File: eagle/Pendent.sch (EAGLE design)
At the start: 39 parts, among them Q1 CMA-4544PF-W, Q2 MPSA42, Q3 8/16/20MHz, U1 MAX9814TDFN14, U2 LF50ABDT-TR, U3 ATMEGA328

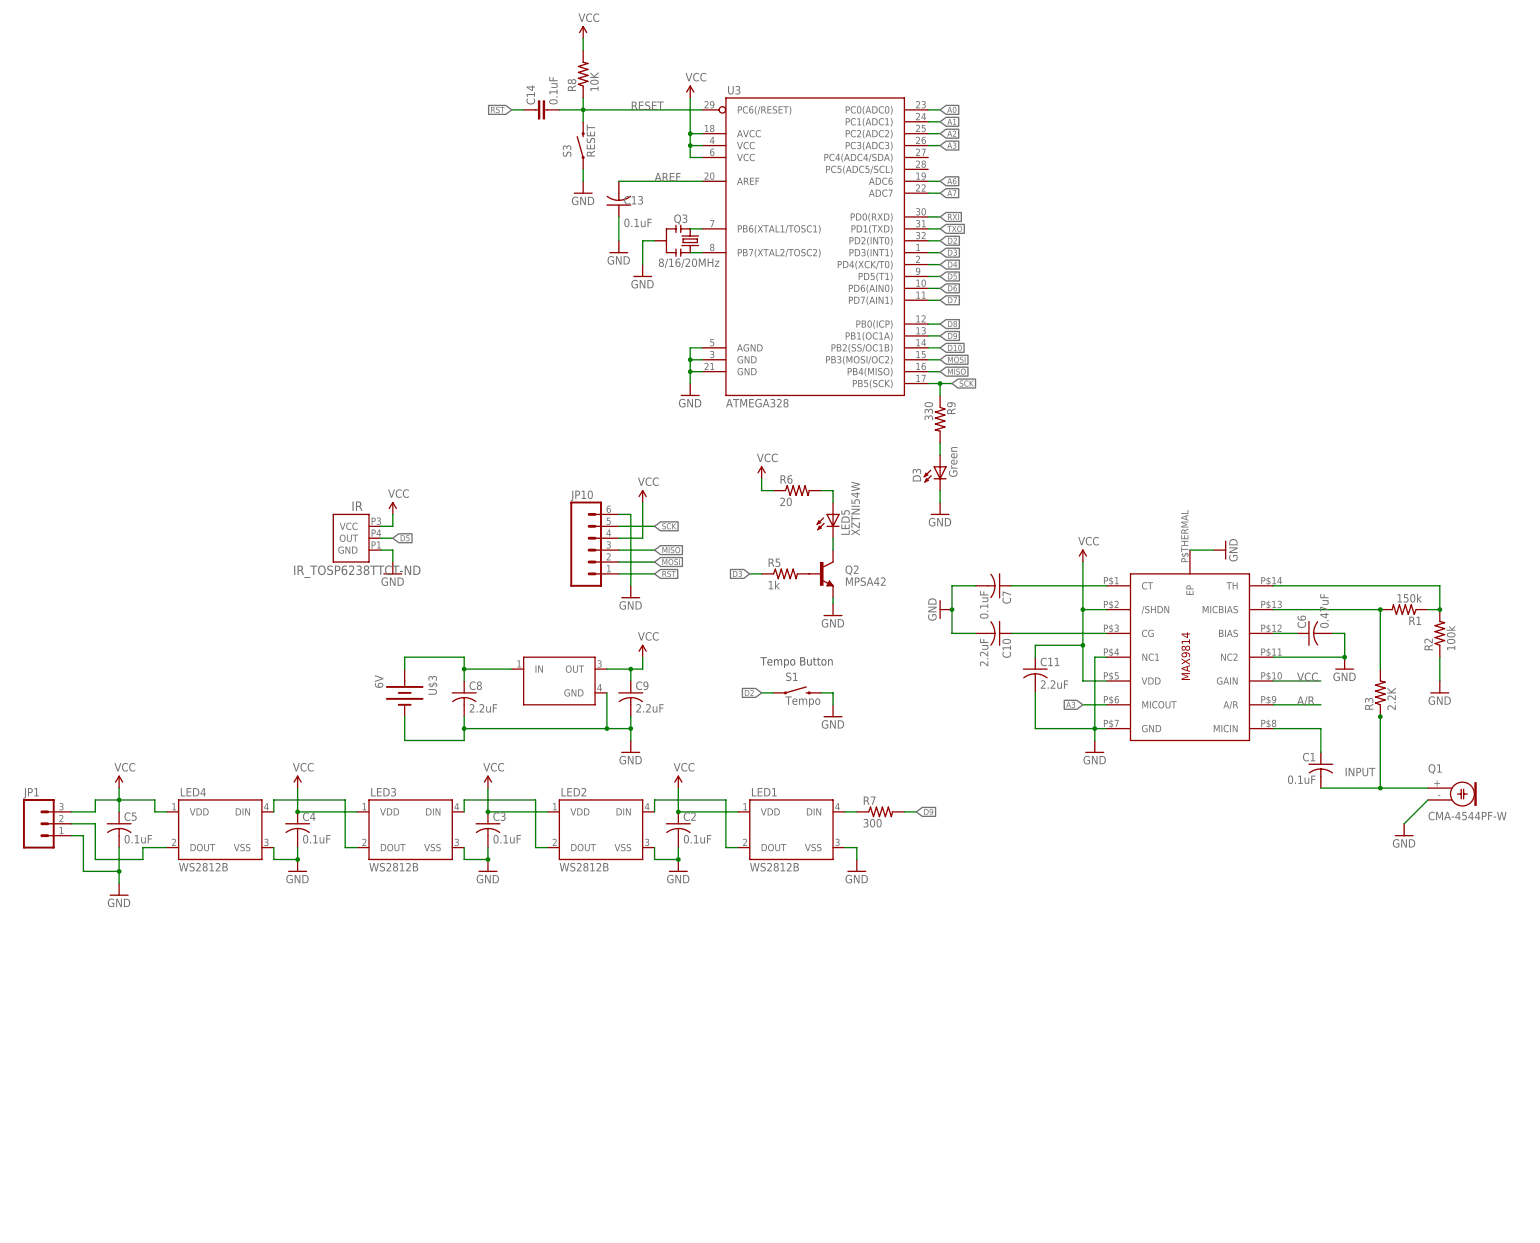
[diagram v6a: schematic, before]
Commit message: Add Push On Button
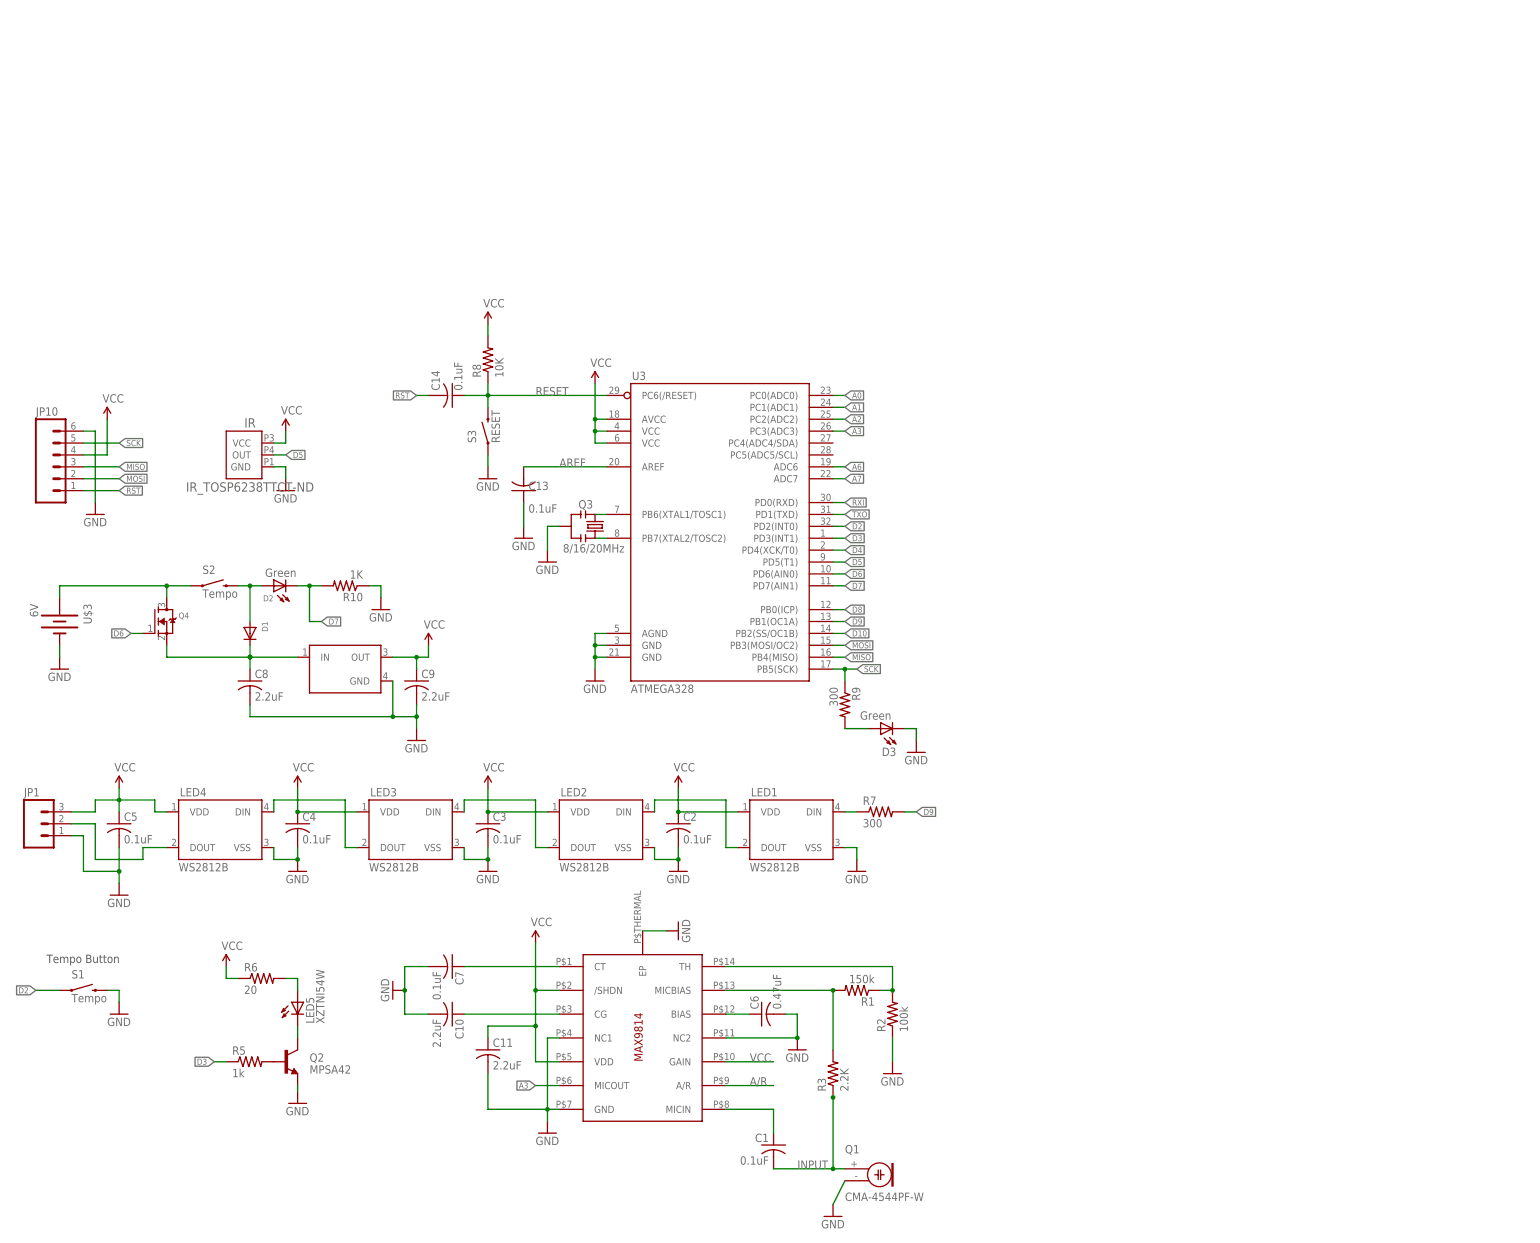
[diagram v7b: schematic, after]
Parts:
- added D1: (no value), adafruit:DIODESMA
- added D2: Green, adafruit:LEDCHIPLED_0805
- added Q4: (no value), adafruit:MOSFET-NREFLOW
- added R10: 1K, adafruit:R-US_R0805
- added S2: Tempo, SparkFun-Electromechanical:SWITCH-MOMENTARY-2SMD-REDUNDANT
- C14: device SparkFun:CAP0603-CAP -> adafruit:C-USC0805K
- R9: value 330 -> 300
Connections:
- removed net VBATT: C8.1, U$3.+, U2.IN
- new net N$20: D1.A, D2.A, S2.2
- new net VBAT: Q4.D, S2.1, U$3.+
- new net VIN: C8.1, D1.C, Q4.S, U2.IN
- net D6: now also Q4.G
- net D7: now also D2.C, R10.2
- net GND: now also R10.1
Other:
- moved on the sheet: C1, C10, C11, C13, C14, C6, C7, C8, C9, D3, IR, JP10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

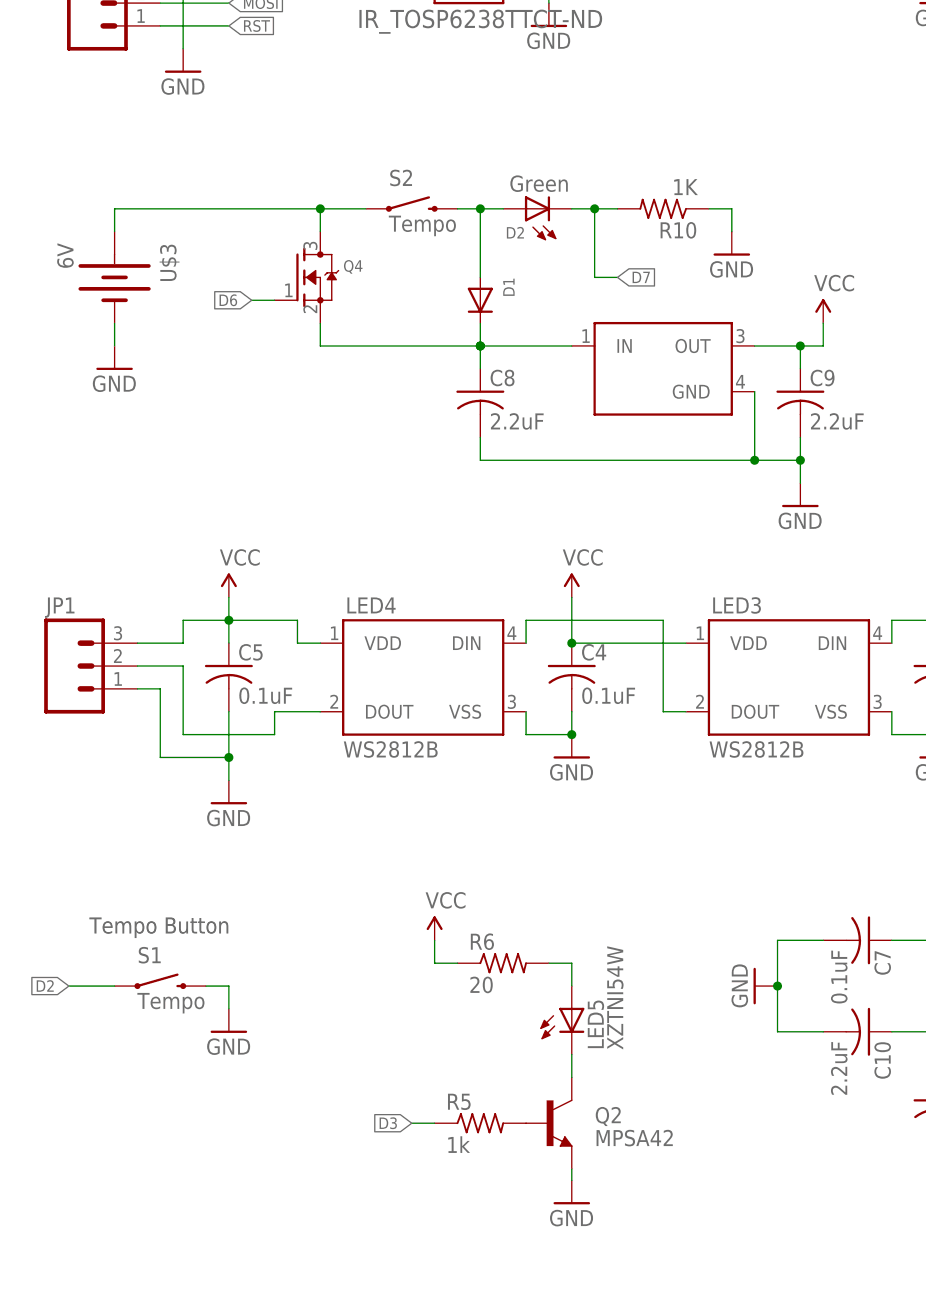
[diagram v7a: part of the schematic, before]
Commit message: Remove non-working mosfet, switch to using power down
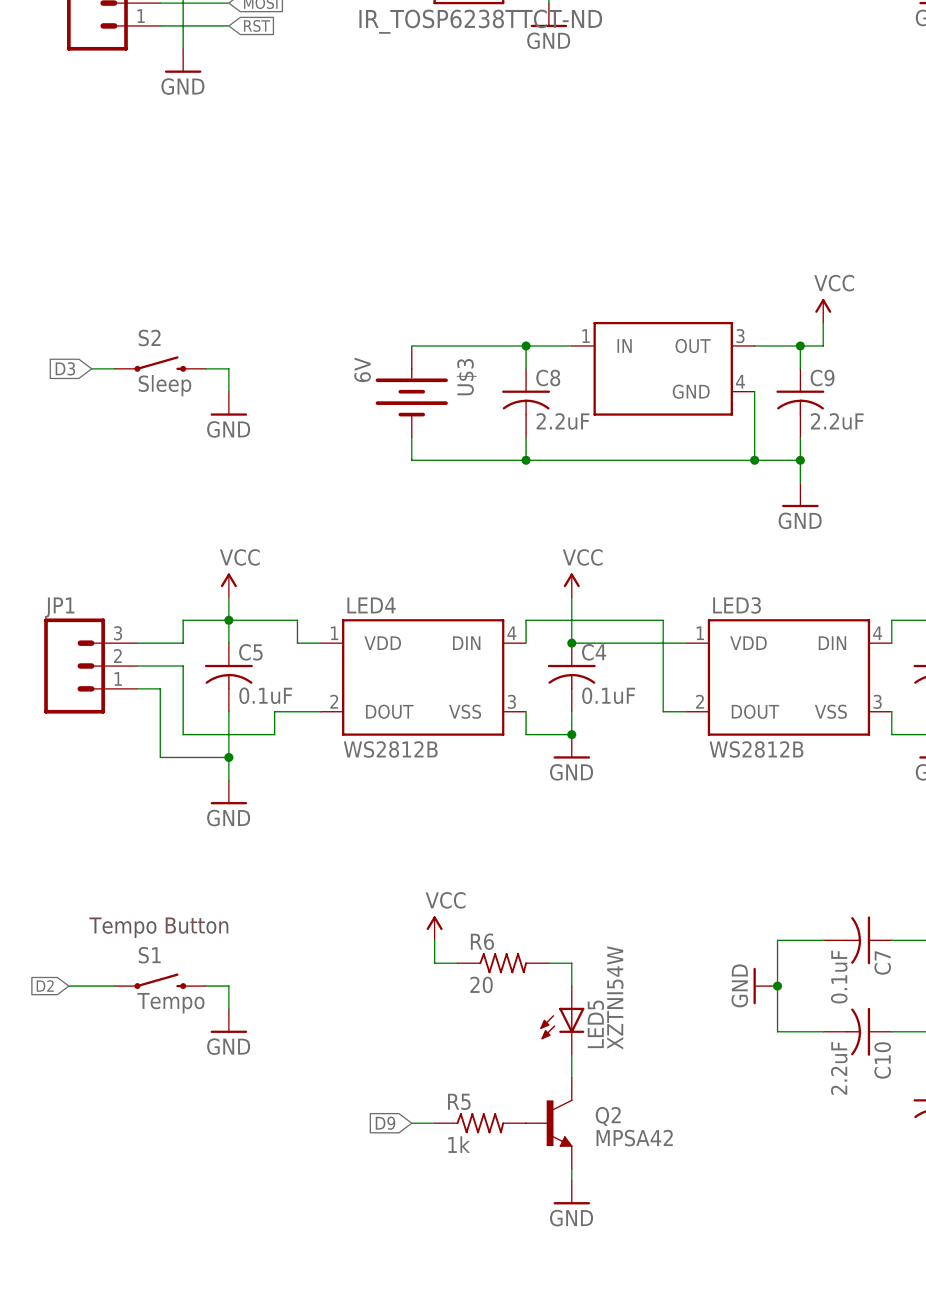
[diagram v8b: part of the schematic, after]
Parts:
- removed D1: (no value), adafruit:DIODESMA
- removed D2: Green, adafruit:LEDCHIPLED_0805
- removed Q4: (no value), adafruit:MOSFET-NREFLOW
- removed R10: 1K, adafruit:R-US_R0805
- S2: value Tempo -> Sleep
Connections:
- removed net N$20: D1.A, D2.A, S2.2
- removed net VBAT: Q4.D, S2.1, U$3.+
- net D3: now also S2.1; no longer R5.1
- net D6: no longer Q4.G
- net D7: no longer D2.C, R10.2
- net D9: now also R5.1
- net GND: now also S2.2; no longer R10.1
- net VIN: now also U$3.+; no longer D1.C, Q4.S
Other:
- moved on the sheet: C8, S2, U$3
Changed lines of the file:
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@@
 <part name="SUPPLY1" library="SparkFun-Aesthetics" deviceset="VCC" device=""/>
 <part name="GND17" library="SparkFun-Aesthetics" deviceset="GND" device=""/>
-<part name="Q4" library="adafruit" deviceset="MOSFET-N" device="REFLOW"/>
-<part name="S2" library="SparkFun-Electromechanical" deviceset="SWITCH-MOMENTARY-2" device="SMD-REDUNDANT" value="Tempo"/>
-<part name="D1" library="adafruit" deviceset="DIODE" device="SMA"/>
-<part name="D2" library="adafruit" deviceset="LED" device="CHIPLED_0805" value="Green"/>
-<part name="R10" library="adafruit" deviceset="R-US_" device="R0805" value="1K"/>
+<part name="S2" library="SparkFun-Electromechanical" deviceset="SWITCH-MOMENTARY-2" device="SMD-REDUNDANT" value="Sleep"/>
 <part name="GND23" library="SparkFun" deviceset="GND" device=""/>
-<part name="GND22" library="SparkFun" deviceset="GND" device=""/>
 </parts>
 <sheets>
@@
 <instance part="C5" gate="G$1" x="-22.86" y="114.3"/>
 <instance part="U2" gate="G$1" x="25.4" y="147.32"/>
-<instance part="U$3" gate="G$1" x="-35.56" y="157.48" rot="R270"/>
-<instance part="C8" gate="G$1" x="5.08" y="144.78"/>
+<instance part="U$3" gate="G$1" x="-2.54" y="144.78" rot="R270"/>
+<instance part="C8" gate="G$1" x="10.16" y="144.78"/>
 <instance part="C9" gate="G$1" x="40.64" y="144.78"/>
 <instance part="C1" gate="G$1" x="116.84" y="45.72" rot="MR0"/>
@@
 <instance part="SUPPLY1" gate="1" x="12.7" y="198.12"/>
 <instance part="GND17" gate="1" x="12.7" y="185.42"/>
-<instance part="Q4" gate="G$1" x="-15.24" y="157.48"/>
-<instance part="S2" gate="G$1" x="-2.54" y="165.1"/>
-<instance part="D1" gate="G$1" x="5.08" y="154.94" rot="R270"/>
-<instance part="D2" gate="G$1" x="10.16" y="165.1" smashed="yes" rot="R90">
-<attribute name="NAME" x="7.874" y="161.798" size="1.27" layer="95"/>
-<attribute name="VALUE" x="14.986" y="168.783" size="1.778" layer="96" rot="R180"/>
-</instance>
-<instance part="R10" gate="G$1" x="25.4" y="165.1" rot="R180"/>
-<instance part="GND23" gate="1" x="33.02" y="160.02"/>
-<instance part="GND22" gate="1" x="-35.56" y="147.32"/>
+<instance part="S2" gate="G$1" x="-30.48" y="147.32"/>
+<instance part="GND23" gate="1" x="-22.86" y="142.24"/>
 </instances>
 <busses>
@@
 <junction x="40.64" y="137.16"/>
 <pinref part="C8" gate="G$1" pin="2"/>
-<wire x1="5.08" y1="137.16" x2="5.08" y2="139.7" width="0.1524" layer="91"/>
-<wire x1="35.56" y1="137.16" x2="5.08" y2="137.16" width="0.1524" layer="91"/>
+<wire x1="10.16" y1="137.16" x2="10.16" y2="139.7" width="0.1524" layer="91"/>
+<wire x1="35.56" y1="137.16" x2="10.16" y2="137.16" width="0.1524" layer="91"/>
 <junction x="35.56" y="137.16"/>
+<pinref part="U$3" gate="G$1" pin="-"/>
+<wire x1="-2.54" y1="137.16" x2="-2.54" y2="139.7" width="0.1524" layer="91"/>
+<wire x1="-2.54" y1="137.16" x2="10.16" y2="137.16" width="0.1524" layer="91"/>
+<junction x="10.16" y="137.16"/>
 </segment>
 <segment>
@@
 </segment>
 <segment>
-<pinref part="R10" gate="G$1" pin="1"/>
-<pinref part="GND23" gate="1" pin="GND"/>
-<wire x1="30.48" y1="165.1" x2="33.02" y2="165.1" width="0.1524" layer="91"/>
-<wire x1="33.02" y1="165.1" x2="33.02" y2="162.56" width="0.1524" layer="91"/>
-</segment>
-<segment>
-<pinref part="U$3" gate="G$1" pin="-"/>
-<wire x1="-35.56" y1="149.86" x2="-35.56" y2="152.4" width="0.1524" layer="91"/>
-<pinref part="GND22" gate="1" pin="GND"/>
-</segment>
-<segment>
 <pinref part="D3" gate="G$1" pin="C"/>
 <pinref part="GND19" gate="1" pin="GND"/>
 <wire x1="144.78" y1="134.62" x2="147.32" y2="134.62" width="0.1524" layer="91"/>
 <wire x1="147.32" y1="134.62" x2="147.32" y2="132.08" width="0.1524" layer="91"/>
+</segment>
+<segment>
+<pinref part="S2" gate="G$1" pin="2"/>
+<pinref part="GND23" gate="1" pin="GND"/>
+<wire x1="-25.4" y1="147.32" x2="-22.86" y2="147.32" width="0.1524" layer="91"/>
+<wire x1="-22.86" y1="147.32" x2="-22.86" y2="144.78" width="0.1524" layer="91"/>
 </segment>
 </net>
@@
 <pinref part="C8" gate="G$1" pin="1"/>
 <pinref part="U2" gate="G$1" pin="IN"/>
-<wire x1="5.08" y1="149.86" x2="5.08" y2="147.32" width="0.1524" layer="91"/>
-<wire x1="15.24" y1="149.86" x2="5.08" y2="149.86" width="0.1524" layer="91"/>
-<pinref part="Q4" gate="G$1" pin="S"/>
-<wire x1="-12.7" y1="152.4" x2="-12.7" y2="149.86" width="0.1524" layer="91"/>
-<wire x1="-12.7" y1="149.86" x2="5.08" y2="149.86" width="0.1524" layer="91"/>
-<junction x="5.08" y="149.86"/>
-<pinref part="D1" gate="G$1" pin="C"/>
-<wire x1="5.08" y1="152.4" x2="5.08" y2="149.86" width="0.1524" layer="91"/>
-<junction x="5.08" y="149.86"/>
+<wire x1="10.16" y1="149.86" x2="10.16" y2="147.32" width="0.1524" layer="91"/>
+<wire x1="15.24" y1="149.86" x2="10.16" y2="149.86" width="0.1524" layer="91"/>
+<pinref part="U$3" gate="G$1" pin="+"/>
+<wire x1="-2.54" y1="149.86" x2="10.16" y2="149.86" width="0.1524" layer="91"/>
+<junction x="10.16" y="149.86"/>
 </segment>
 </net>
@@
 <label x="147.32" y="116.84" size="1.27" layer="95" xref="yes"/>
 </segment>
+<segment>
+<pinref part="R5" gate="G$1" pin="1"/>
+<wire x1="0" y1="63.5" x2="-2.54" y2="63.5" width="0.1524" layer="91"/>
+<label x="-2.54" y="63.5" size="1.4224" layer="95" rot="R180" xref="yes"/>
+</segment>
 </net>
 <net name="D8" class="0">
@@
 </segment>
 <segment>
-<pinref part="R5" gate="G$1" pin="1"/>
-<wire x1="-2.54" y1="63.5" x2="0" y2="63.5" width="0.1524" layer="91"/>
-<label x="-2.54" y="63.5" size="1.27" layer="95" rot="R180" xref="yes"/>
+<pinref part="S2" gate="G$1" pin="1"/>
+<wire x1="-35.56" y1="147.32" x2="-38.1" y2="147.32" width="0.1524" layer="91"/>
+<label x="-38.1" y="147.32" size="1.4224" layer="95" rot="R180" xref="yes"/>
 </segment>
 </net>
@@
 <label x="132.08" y="167.64" size="1.27" layer="95" xref="yes"/>
 </segment>
-<segment>
-<pinref part="Q4" gate="G$1" pin="G"/>
-<wire x1="-17.78" y1="154.94" x2="-20.32" y2="154.94" width="0.1524" layer="91"/>
-<label x="-20.32" y="154.94" size="1.27" layer="95" rot="R180" xref="yes"/>
-</segment>
 </net>
 <net name="D7" class="0">
@@
 <pinref part="U3" gate="G$1" pin="PD7(AIN1)"/>
 <label x="132.08" y="165.1" size="1.27" layer="95" xref="yes"/>
-</segment>
-<segment>
-<pinref part="D2" gate="G$1" pin="C"/>
-<pinref part="R10" gate="G$1" pin="2"/>
-<wire x1="15.24" y1="165.1" x2="17.78" y2="165.1" width="0.1524" layer="91"/>
-<wire x1="17.78" y1="165.1" x2="20.32" y2="165.1" width="0.1524" layer="91"/>
-<wire x1="17.78" y1="165.1" x2="17.78" y2="157.48" width="0.1524" layer="91"/>
-<junction x="17.78" y="165.1"/>
-<wire x1="17.78" y1="157.48" x2="20.32" y2="157.48" width="0.1524" layer="91"/>
-<label x="20.32" y="157.48" size="1.27" layer="95" xref="yes"/>
 </segment>
 </net>
@@
 </segment>
 </net>
-<net name="VBAT" class="0">
-<segment>
-<pinref part="U$3" gate="G$1" pin="+"/>
-<pinref part="S2" gate="G$1" pin="1"/>
-<wire x1="-35.56" y1="162.56" x2="-35.56" y2="165.1" width="0.1524" layer="91"/>
-<wire x1="-35.56" y1="165.1" x2="-12.7" y2="165.1" width="0.1524" layer="91"/>
-<wire x1="-12.7" y1="165.1" x2="-7.62" y2="165.1" width="0.1524" layer="91"/>
-<pinref part="Q4" gate="G$1" pin="D"/>
-<wire x1="-12.7" y1="165.1" x2="-12.7" y2="162.56" width="0.1524" layer="91"/>
-<junction x="-12.7" y="165.1"/>
-</segment>
-</net>
-<net name="N$20" class="0">
-<segment>
-<pinref part="S2" gate="G$1" pin="2"/>
-<wire x1="2.54" y1="165.1" x2="5.08" y2="165.1" width="0.1524" layer="91"/>
-<pinref part="D1" gate="G$1" pin="A"/>
-<wire x1="5.08" y1="165.1" x2="5.08" y2="157.48" width="0.1524" layer="91"/>
-<junction x="5.08" y="165.1"/>
-<pinref part="D2" gate="G$1" pin="A"/>
-<wire x1="5.08" y1="165.1" x2="7.62" y2="165.1" width="0.1524" layer="91"/>
-</segment>
-</net>
